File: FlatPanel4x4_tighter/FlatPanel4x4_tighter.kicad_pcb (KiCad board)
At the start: 2 copper layers, 186 x 226 mm, 116 parts

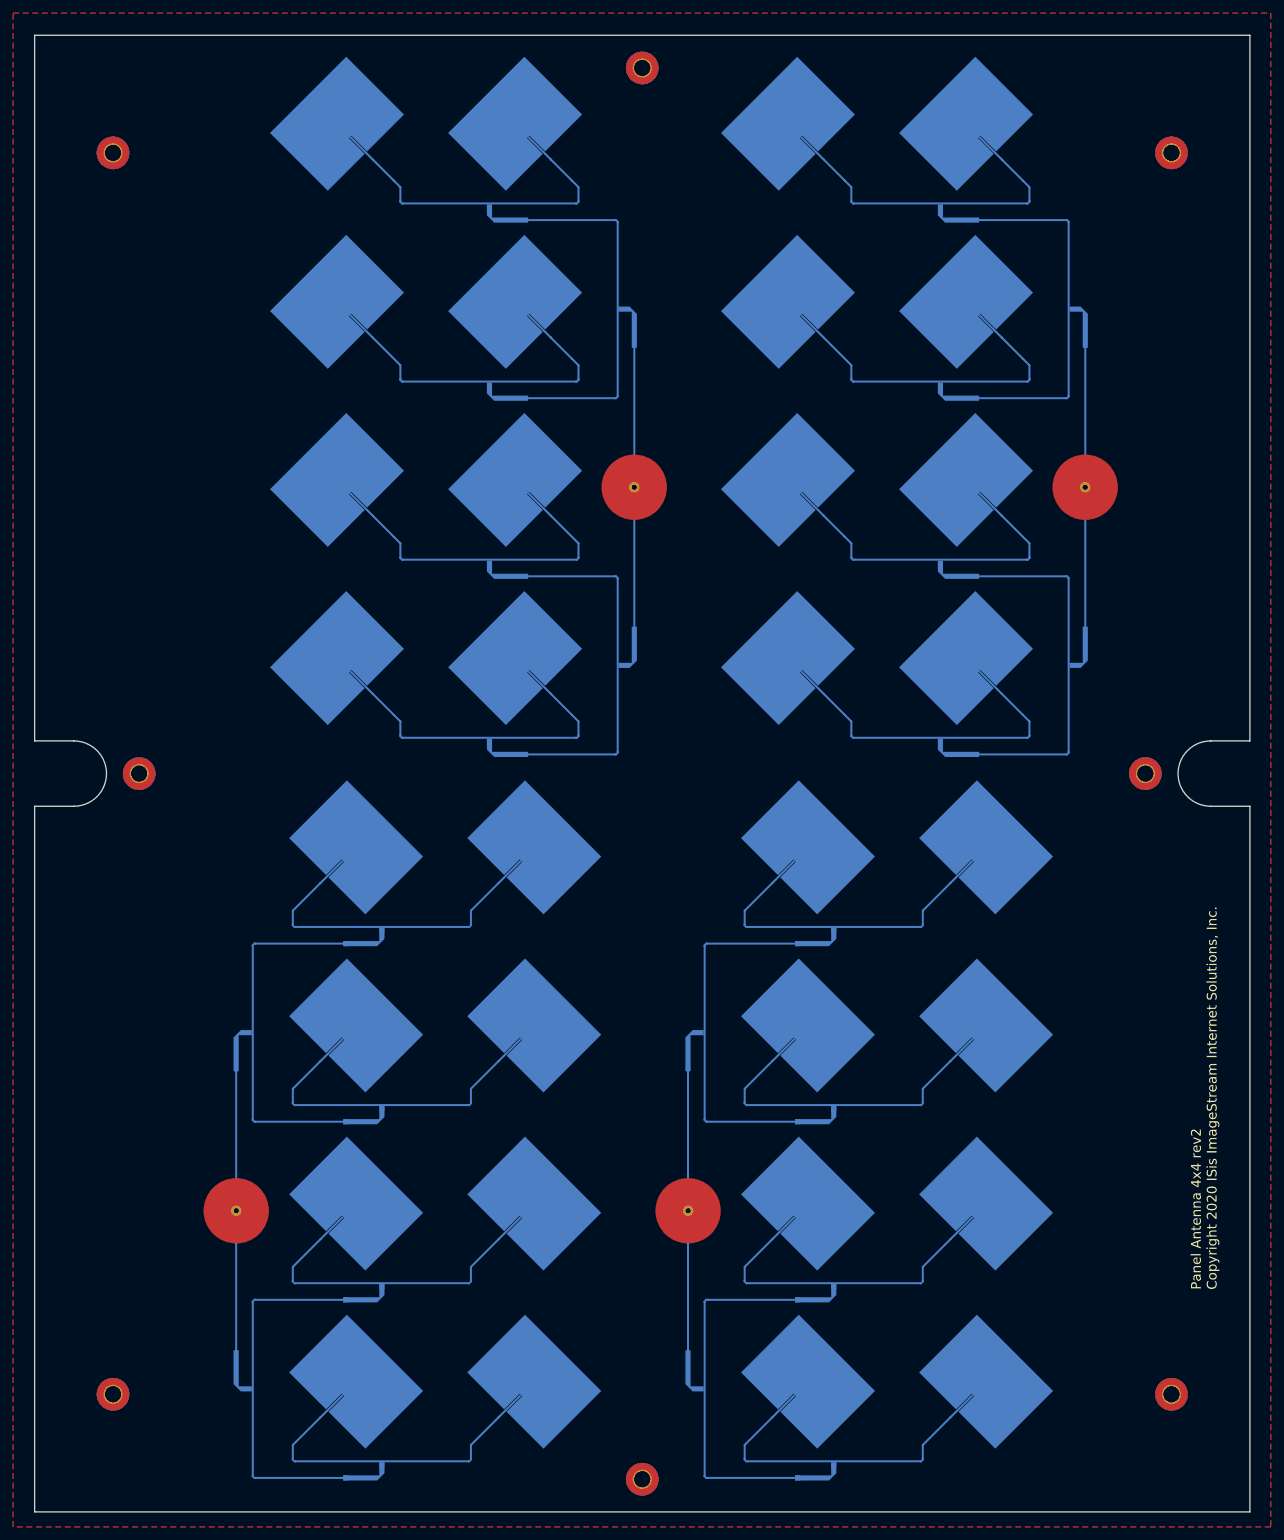
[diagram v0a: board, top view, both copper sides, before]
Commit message: Placed an order with JLCPCB for the Tighter 4pol version and the "Dual XPol" which actually was aperture coupled.
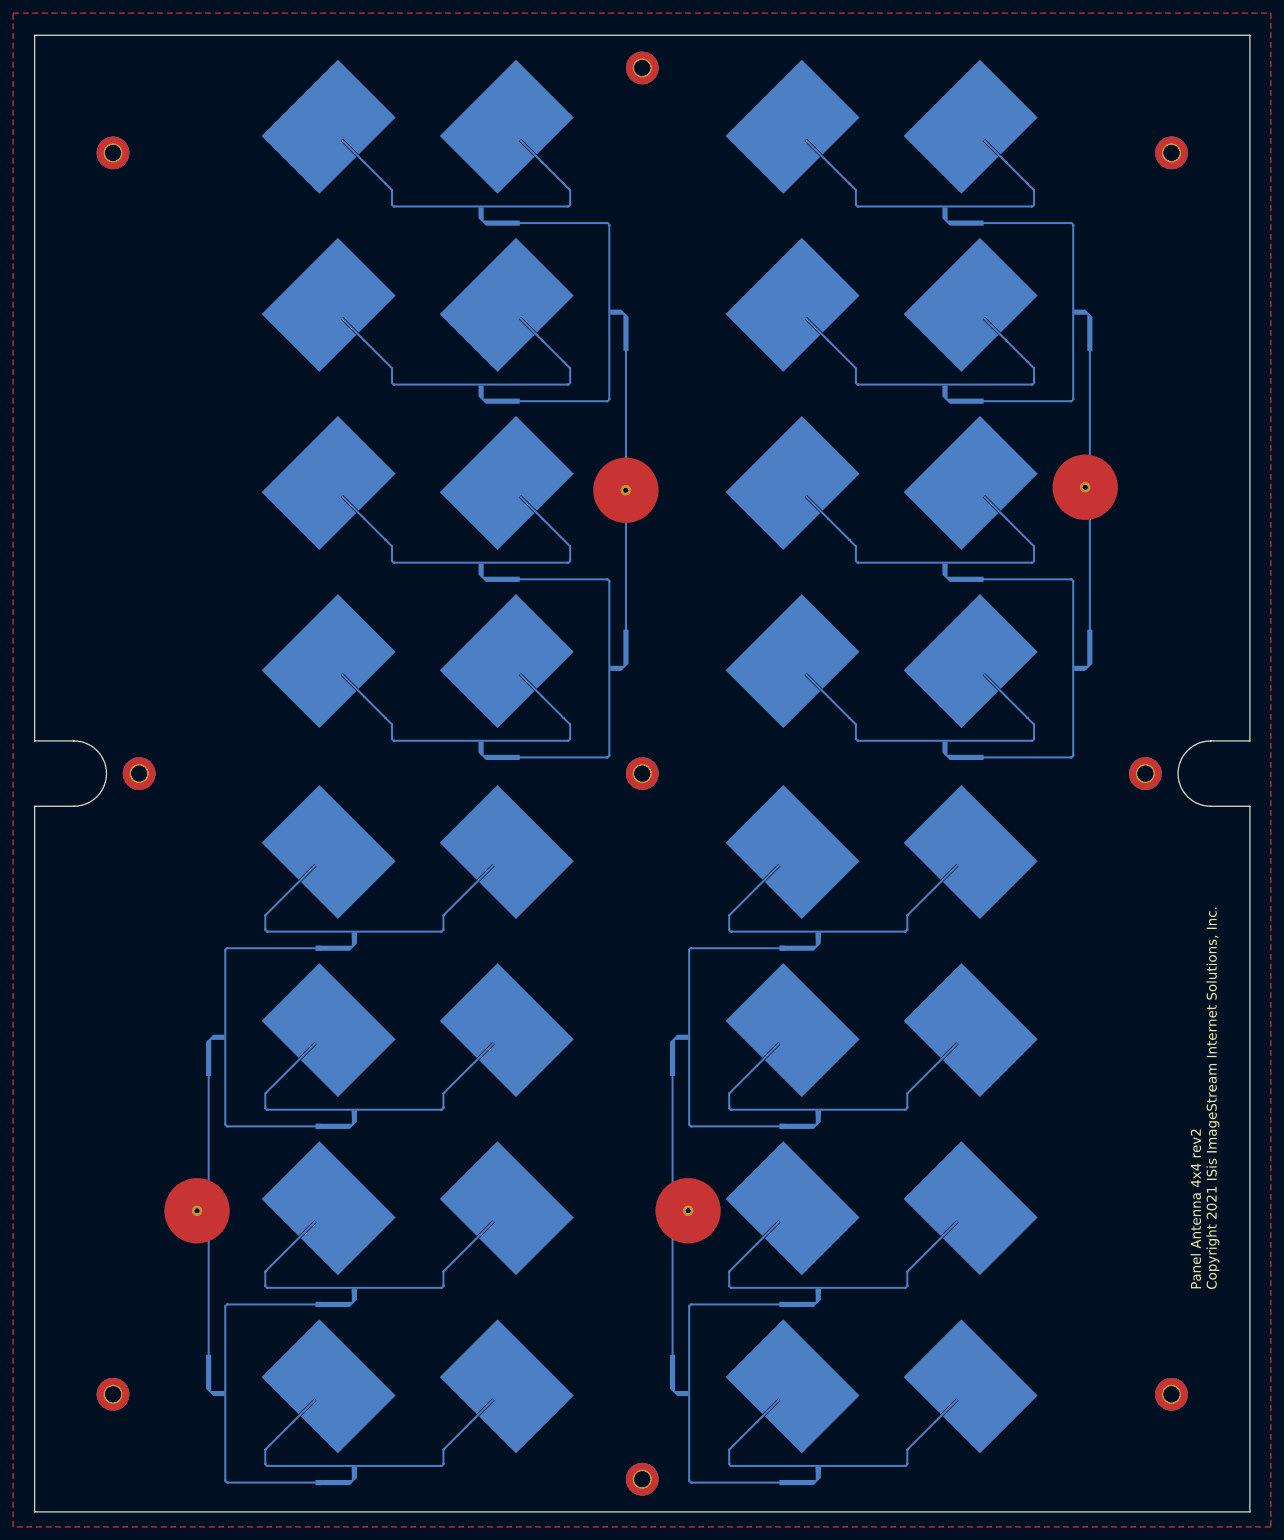
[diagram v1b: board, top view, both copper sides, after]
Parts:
- added H11: Mounting Hole, MountingHole:MountingHole_2.5mm_Pad_TopBottom, F.Cu at (93.0, 113.0)
- moved Feed3 6.00 mm to (24.9, 179.9)
- moved REF** 4.27 mm to (48.9, 194.2)
- moved REF** 4.27 mm to (48.9, 167.0)
- moved REF** 4.27 mm to (48.9, 221.5)
- moved REF** 4.27 mm to (48.9, 139.7)
- moved AA5 4.27 mm to (35.3, 219.0)
- moved AA5 4.27 mm to (35.3, 191.7)
- moved AA5 4.27 mm to (29.2, 167.0)
- moved AA5 4.27 mm to (62.6, 219.0)
- moved AA5 4.27 mm to (29.2, 194.2)
- moved AA5 4.27 mm to (62.6, 191.7)
- moved AA5 4.27 mm to (62.6, 137.2)
- moved AA5 4.27 mm to (35.3, 137.2)
- moved AE5 4.27 mm to (45.0, 179.5)
- moved AE6 4.27 mm to (45.0, 206.8)
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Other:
- board text added: "Panel Antenna 4x4 rev2 Copyright 2021 ISis ImageStream Internet Solutions, Inc."
- board text removed: "Panel Antenna 4x4 rev2 Copyright 2020 ISis ImageStream Internet Solutions, Inc."
